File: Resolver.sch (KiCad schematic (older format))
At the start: 11 parts, among them SW1 SW_DIP_x02, U6 AD2S1200YSTZ, Y2 8.912 MHZ

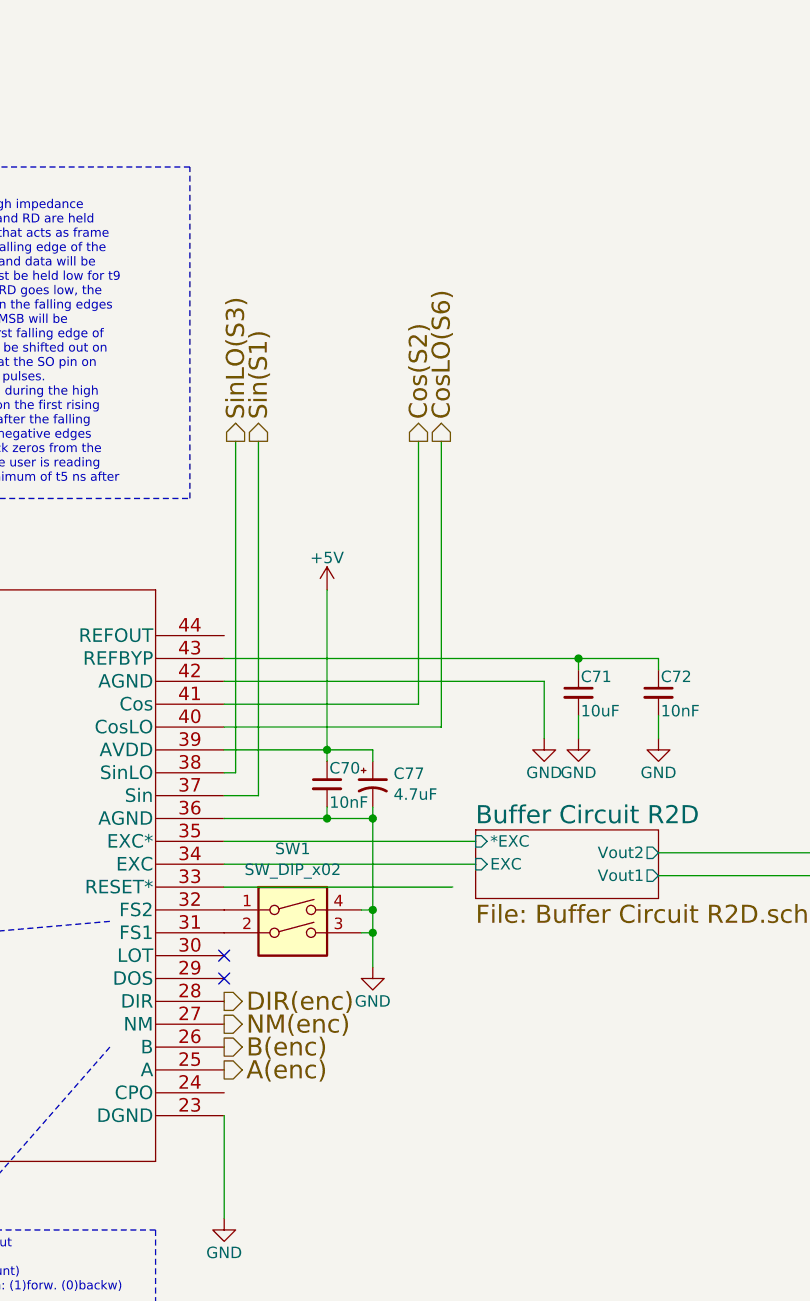
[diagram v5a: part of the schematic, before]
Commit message: -started implementing new sin/cos-Encoder Inputs -small changes like silkscreen
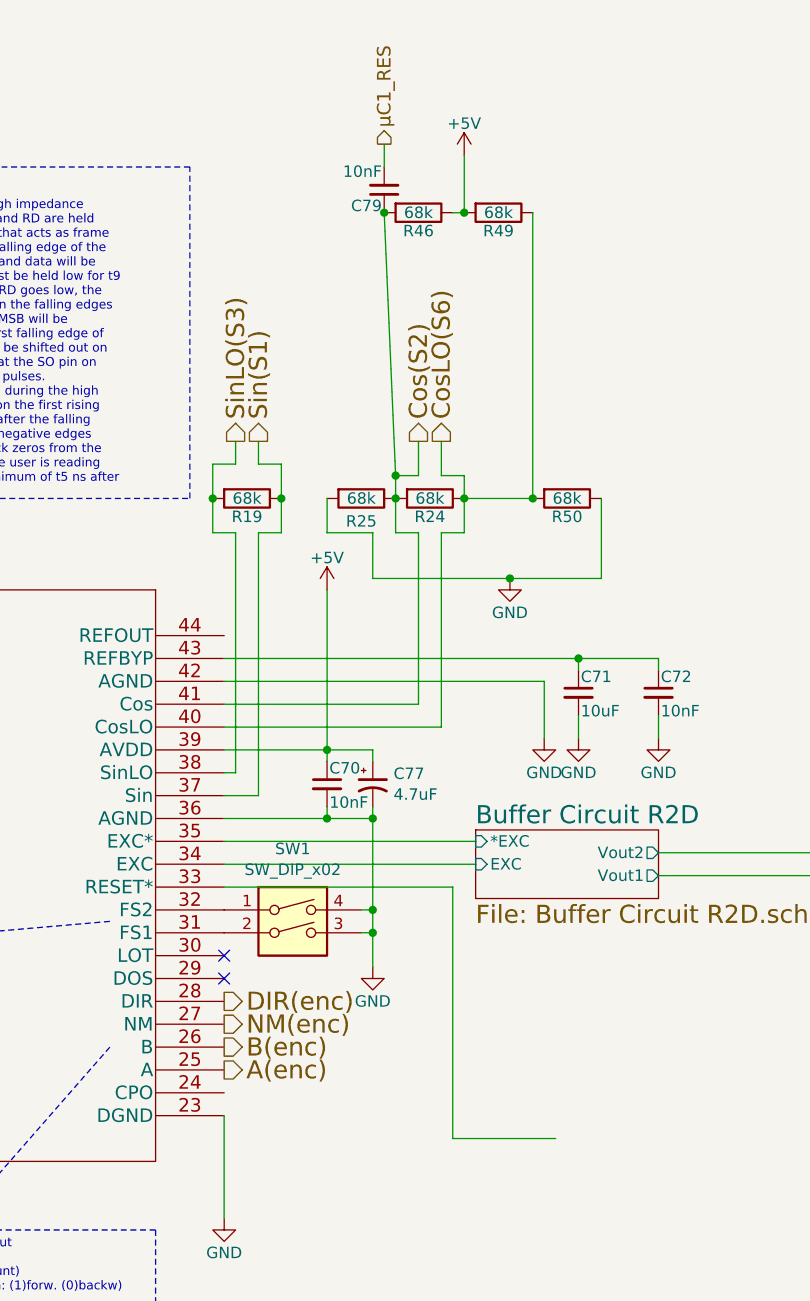
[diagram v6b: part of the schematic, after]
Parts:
- added C79: 10nF, Capacitor_SMD:C_0805_2012Metric, symbol Amalga_100-rescue:C_Small-Device
- added R19, R24, R25, R46, R49, R50: 68k, Resistor_SMD:R_0805_2012Metric, symbol Amalga_100-rescue:R-Device
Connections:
- net +5V: now also R46.1, R49.2
- net Cos(S2): now also C79.1, R24.2, R25.1, R46.2
- net CosLO(S6): now also R24.1, R49.1, R50.2
- net GND: now also R25.2, R50.1
- net Sin(S1): now also R19.1
- net SinLO(S3): now also R19.2
- new net µC1_RES: C79.2
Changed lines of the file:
@@
 EESchema Schematic File Version 4
 LIBS:Amalga_100-cache
-EELAYER 29 0
+EELAYER 26 0
 EELAYER END
 $Descr A4 11693 8268
@@
 	5850 3100 6700 3100
 Wire Wire Line
-	6700 3100 6700 1950
+	6700 3100 6700 2350
 Wire Wire Line
 	5850 3200 6800 3200
 Wire Wire Line
-	6800 3200 6800 1950
+	6800 3200 6800 2350
 Wire Wire Line
 	5850 3400 5900 3400
 Wire Wire Line
-	5900 3400 5900 1950
+	5900 3400 5900 2350
 Wire Wire Line
 	5850 3500 6000 3500
 Wire Wire Line
-	6000 1950 6000 3500
+	6000 1950 6000 2050
 Connection ~ 2150 5050
 $Comp
@@
 Wire Wire Line
 	2700 4300 2700 4550
+Wire Wire Line
+	6850 3900 6850 5000
+Wire Wire Line
+	6850 5000 7300 5000
+Wire Wire Line
+	5900 2350 5800 2350
+Wire Wire Line
+	5800 2050 5900 2050
+Wire Wire Line
+	5900 2050 5900 1950
+Wire Wire Line
+	6000 2050 6100 2050
+Wire Wire Line
+	6100 2350 6000 2350
+Wire Wire Line
+	6000 2350 6000 3500
+$Comp
+L Amalga_100-rescue:R-Device R?
+U 1 1 5CC156E1
+P 5950 2200
+AR Path="/5CC156E1" Ref="R?"  Part="1"
+AR Path="/5C9D0FFC/5CC156E1" Ref="R19"  Part="1"
+F 0 "R19" V 6030 2200 50  0000 C CNN
+F 1 "68k" V 5950 2200 50  0000 C CNN
+F 2 "Resistor_SMD:R_0805_2012Metric" V 5880 2200 30  0001 C CNN
+F 3 "" H 5950 2200 30  0000 C CNN
+	1    5950 2200
+	0    1    1    0
+$EndComp
+Wire Wire Line
+	5800 2200 5800 2050
+Wire Wire Line
+	5800 2350 5800 2200
+Connection ~ 5800 2200
+Wire Wire Line
+	6100 2200 6100 2350
+Wire Wire Line
+	6100 2050 6100 2200
+Connection ~ 6100 2200
+$Comp
+L Amalga_100-rescue:R-Device R?
+U 1 1 5CC24437
+P 6750 2200
+AR Path="/5CC24437" Ref="R?"  Part="1"
+AR Path="/5C9D0FFC/5CC24437" Ref="R24"  Part="1"
+F 0 "R24" V 6830 2200 50  0000 C CNN
+F 1 "68k" V 6750 2200 50  0000 C CNN
+F 2 "Resistor_SMD:R_0805_2012Metric" V 6680 2200 30  0001 C CNN
+F 3 "" H 6750 2200 30  0000 C CNN
+	1    6750 2200
+	0    1    1    0
+$EndComp
+Wire Wire Line
+	6800 2100 6900 2100
+Wire Wire Line
+	6900 2100 6900 2200
+Wire Wire Line
+	6800 2100 6800 1950
+Wire Wire Line
+	6900 2200 6900 2350
+Wire Wire Line
+	6900 2350 6800 2350
+Connection ~ 6900 2200
+Wire Wire Line
+	6700 2350 6600 2350
+Wire Wire Line
+	6600 2350 6600 2200
+Wire Wire Line
+	6600 2200 6600 2100
+Wire Wire Line
+	6600 2100 6700 2100
+Connection ~ 6600 2200
+Wire Wire Line
+	6700 2100 6700 1950
+Wire Wire Line
+	6900 2200 7200 2200
+Wire Wire Line
+	7200 2200 7200 950
+Connection ~ 6600 2100
+$Comp
+L Amalga_100-rescue:R-Device R?
+U 1 1 5CC34D88
+P 7050 950
+AR Path="/5CC34D88" Ref="R?"  Part="1"
+AR Path="/5C9D0FFC/5CC34D88" Ref="R49"  Part="1"
+F 0 "R49" V 7130 950 50  0000 C CNN
+F 1 "68k" V 7050 950 50  0000 C CNN
+F 2 "Resistor_SMD:R_0805_2012Metric" V 6980 950 30  0001 C CNN
+F 3 "" H 7050 950 30  0000 C CNN
+	1    7050 950
+	0    1    1    0
+$EndComp
+$Comp
+L Amalga_100-rescue:R-Device R?
+U 1 1 5CC39EA6
+P 6700 950
+AR Path="/5CC39EA6" Ref="R?"  Part="1"
+AR Path="/5C9D0FFC/5CC39EA6" Ref="R46"  Part="1"
+F 0 "R46" V 6780 950 50  0000 C CNN
+F 1 "68k" V 6700 950 50  0000 C CNN
+F 2 "Resistor_SMD:R_0805_2012Metric" V 6630 950 30  0001 C CNN
+F 3 "" H 6700 950 30  0000 C CNN
+	1    6700 950
+	0    1    1    0
+$EndComp
+Wire Wire Line
+	6550 950  6600 2100
+Wire Wire Line
+	6850 950  6900 950
+Wire Wire Line
+	6900 950  6900 700
+$Comp
+L Amalga_100-rescue:+5V-power #PWR?
+U 1 1 5CC58225
+P 6900 700
+AR Path="/5899E25F/5CC58225" Ref="#PWR?"  Part="1"
+AR Path="/5C9D0FFC/5CC58225" Ref="#PWR0150"  Part="1"
+F 0 "#PWR0150" H 6900 550 50  0001 C CNN
+F 1 "+5V" H 6900 840 50  0000 C CNN
+F 2 "" H 6900 700 50  0000 C CNN
+F 3 "" H 6900 700 50  0000 C CNN
+	1    6900 700
+	1    0    0    -1
+$EndComp
+Connection ~ 6900 950
+$Comp
+L Amalga_100-rescue:R-Device R?
+U 1 1 5CC619C4
+P 7350 2200
+AR Path="/5CC619C4" Ref="R?"  Part="1"
+AR Path="/5C9D0FFC/5CC619C4" Ref="R50"  Part="1"
+F 0 "R50" V 7430 2200 50  0000 C CNN
+F 1 "68k" V 7350 2200 50  0000 C CNN
+F 2 "Resistor_SMD:R_0805_2012Metric" V 7280 2200 30  0001 C CNN
+F 3 "" H 7350 2200 30  0000 C CNN
+	1    7350 2200
+	0    1    1    0
+$EndComp
+$Comp
+L Amalga_100-rescue:R-Device R?
+U 1 1 5CC619CB
+P 6450 2200
+AR Path="/5CC619CB" Ref="R?"  Part="1"
+AR Path="/5C9D0FFC/5CC619CB" Ref="R25"  Part="1"
+F 0 "R25" V 6550 2200 50  0000 C CNN
+F 1 "68k" V 6450 2200 50  0000 C CNN
+F 2 "Resistor_SMD:R_0805_2012Metric" V 6380 2200 30  0001 C CNN
+F 3 "" H 6450 2200 30  0000 C CNN
+	1    6450 2200
+	0    1    1    0
+$EndComp
+Connection ~ 7200 2200
+Wire Wire Line
+	6300 2200 6300 2350
+Wire Wire Line
+	6300 2350 6500 2350
+Wire Wire Line
+	6500 2550 7100 2550
+Wire Wire Line
+	7500 2550 7500 2200
+Wire Wire Line
+	6500 2350 6500 2550
+$Comp
+L Amalga_100-rescue:GND-power #PWR?
+U 1 1 5CC6E18D
+P 7100 2550
+AR Path="/5895E6A0/5CC6E18D" Ref="#PWR?"  Part="1"
+AR Path="/5C9D0FFC/5CC6E18D" Ref="#PWR0151"  Part="1"
+F 0 "#PWR0151" H 7100 2300 50  0001 C CNN
+F 1 "GND" H 7100 2400 50  0000 C CNN
+F 2 "" H 7100 2550 50  0000 C CNN
+F 3 "" H 7100 2550 50  0000 C CNN
+	1    7100 2550
+	1    0    0    -1
+$EndComp
+Connection ~ 7100 2550
+Wire Wire Line
+	7100 2550 7500 2550
+Text HLabel 6550 650  1    59   Output ~ 0
+µC1_RES
+Connection ~ 6550 950
+$Comp
+L Amalga_100-rescue:C_Small-Device C?
+U 1 1 5CC78ED9
+P 6550 850
+AR Path="/5895E6A0/5CC78ED9" Ref="C?"  Part="1"
+AR Path="/5C9D0FFC/5CC78ED9" Ref="C79"  Part="1"
+F 0 "C79" H 6560 920 50  0000 L CNN
+F 1 "10nF" H 6560 770 50  0000 L CNN
+F 2 "Capacitor_SMD:C_0805_2012Metric" H 6550 850 50  0001 C CNN
+F 3 "" H 6550 850 50  0000 C CNN
+	1    6550 850
+	-1   0    0    1
+$EndComp
+Wire Wire Line
+	6550 750  6550 650
 $EndSCHEMATC

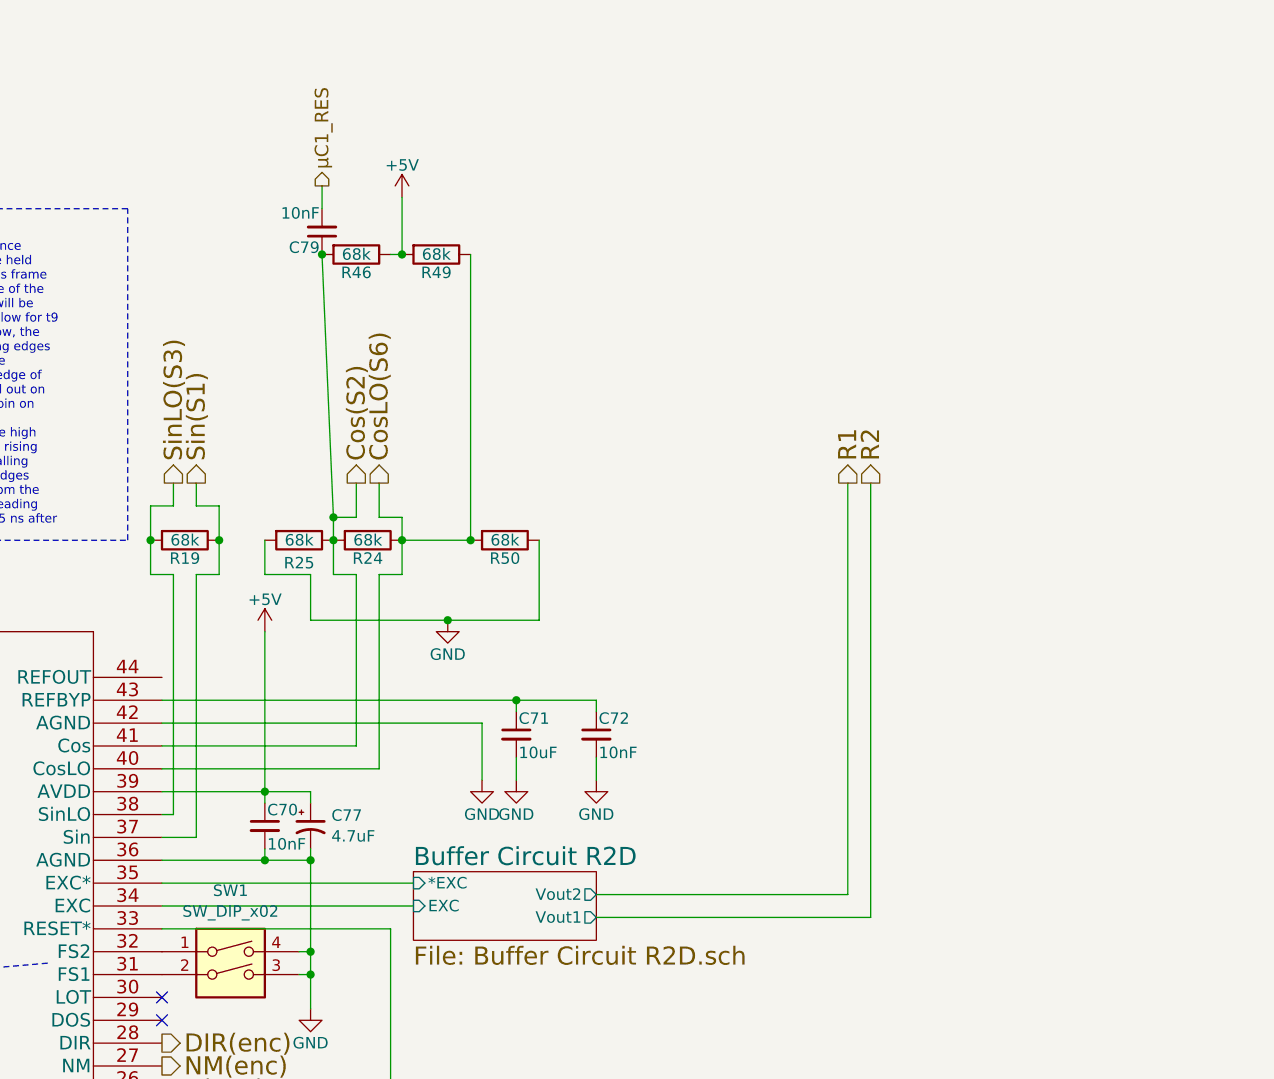
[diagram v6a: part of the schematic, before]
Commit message: added dc-bias for adc sin/cos resolver
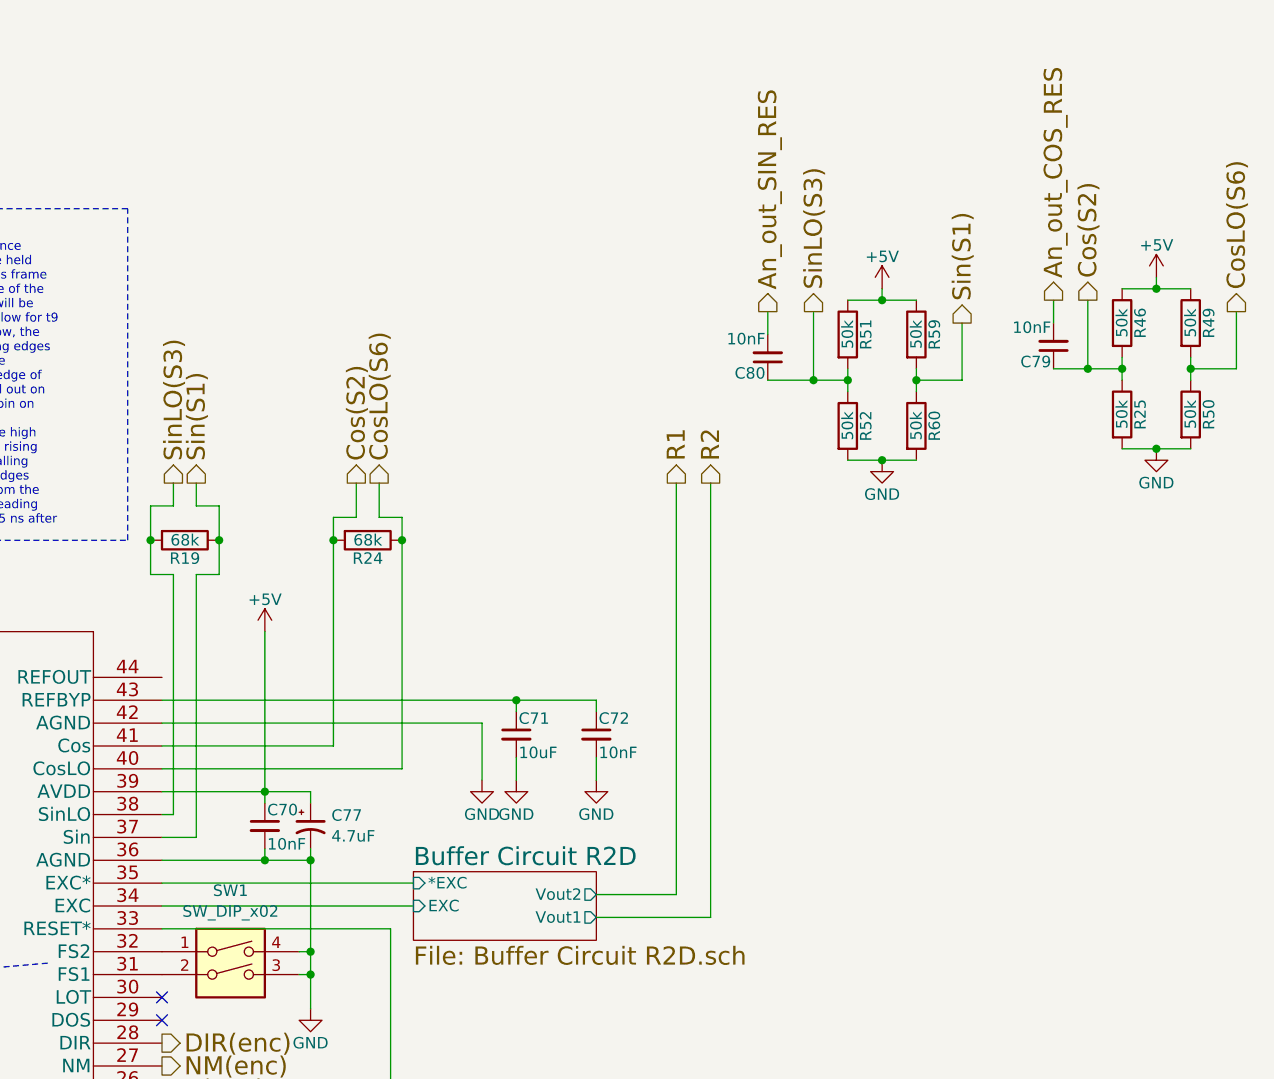
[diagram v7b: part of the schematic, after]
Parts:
- added C80: 10nF, Capacitor_SMD:C_0805_2012Metric, symbol Amalga_100-rescue:C_Small-Device
- added R51, R52, R59, R60: 50k, Resistor_SMD:R_0805_2012Metric, symbol Amalga_100-rescue:R-Device
- R25, R46, R49, R50: value 68k -> 50k
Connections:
- net +5V: now also R49.1, R51.1, R59.1; no longer R49.2
- net CosLO(S6): now also R49.2, R50.1; no longer R49.1, R50.2
- net GND: now also R50.2, R52.2, R60.2; no longer R50.1
- net Sin(S1): now also R59.2, R60.1
- net SinLO(S3): now also C80.1, R51.2, R52.1
- net µC1_RES renamed An_out_COS_RES
- new net An_out_SIN_RES: C80.2
